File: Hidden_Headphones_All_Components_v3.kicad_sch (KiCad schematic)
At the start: 9 parts, among them SW1 SW_Push, SW2 SW_Push, U1 ESP32-S3-MINI-1, U2 PCM5102A, U3 TP4056-42-ESOP8

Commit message: worked on pcb
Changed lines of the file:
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@@
-	)
-	(symbol
-		(lib_id "power:+5V")
-		(at 36.83 45.72 0)
-		(unit 1)
-		(body_style 1)
-		(exclude_from_sim no)
-		(in_bom yes)
-		(on_board yes)
-		(in_pos_files yes)
-		(dnp no)
-		(fields_autoplaced yes)
-		(property "Reference" "#PWR01"
-			(at 36.83 49.53 0)
-			(hide yes)
-			(show_name no)
-			(do_not_autoplace no)
-			(effects
-				(font
-					(size 1.27 1.27)
-				)
-			)
-		)
-		(property "Value" "+5V"
-			(at 36.83 40.64 0)
-			(show_name no)
-			(do_not_autoplace no)
-			(effects
-				(font
-					(size 1.27 1.27)
-				)
-			)
-		)
-		(property "Footprint" ""
-			(at 36.83 45.72 0)
-			(hide yes)
-			(show_name no)
-			(do_not_autoplace no)
-			(effects
-				(font
-					(size 1.27 1.27)
-				)
-			)
-		)
-		(property "Datasheet" ""
-			(at 36.83 45.72 0)
-			(hide yes)
-			(show_name no)
-			(do_not_autoplace no)
-			(effects
-				(font
-					(size 1.27 1.27)
-				)
-			)
-		)
-		(property "Description" "Power symbol creates a global label with name \"+5V\""
-			(at 36.83 45.72 0)
-			(hide yes)
-			(show_name no)
-			(do_not_autoplace no)
-			(effects
-				(font
-					(size 1.27 1.27)
-				)
-			)
-		)
-		(pin "1"
-		)
-		(instances
-			(project "Hidden_Headphones_All_Components_v3"
-				(path "/229b286c-fec7-4b98-8d6c-8cdc215e0cc6"
-					(reference "#PWR01")
-					(unit 1)
-				)
-			)
-		)
 	)
 	(symbol

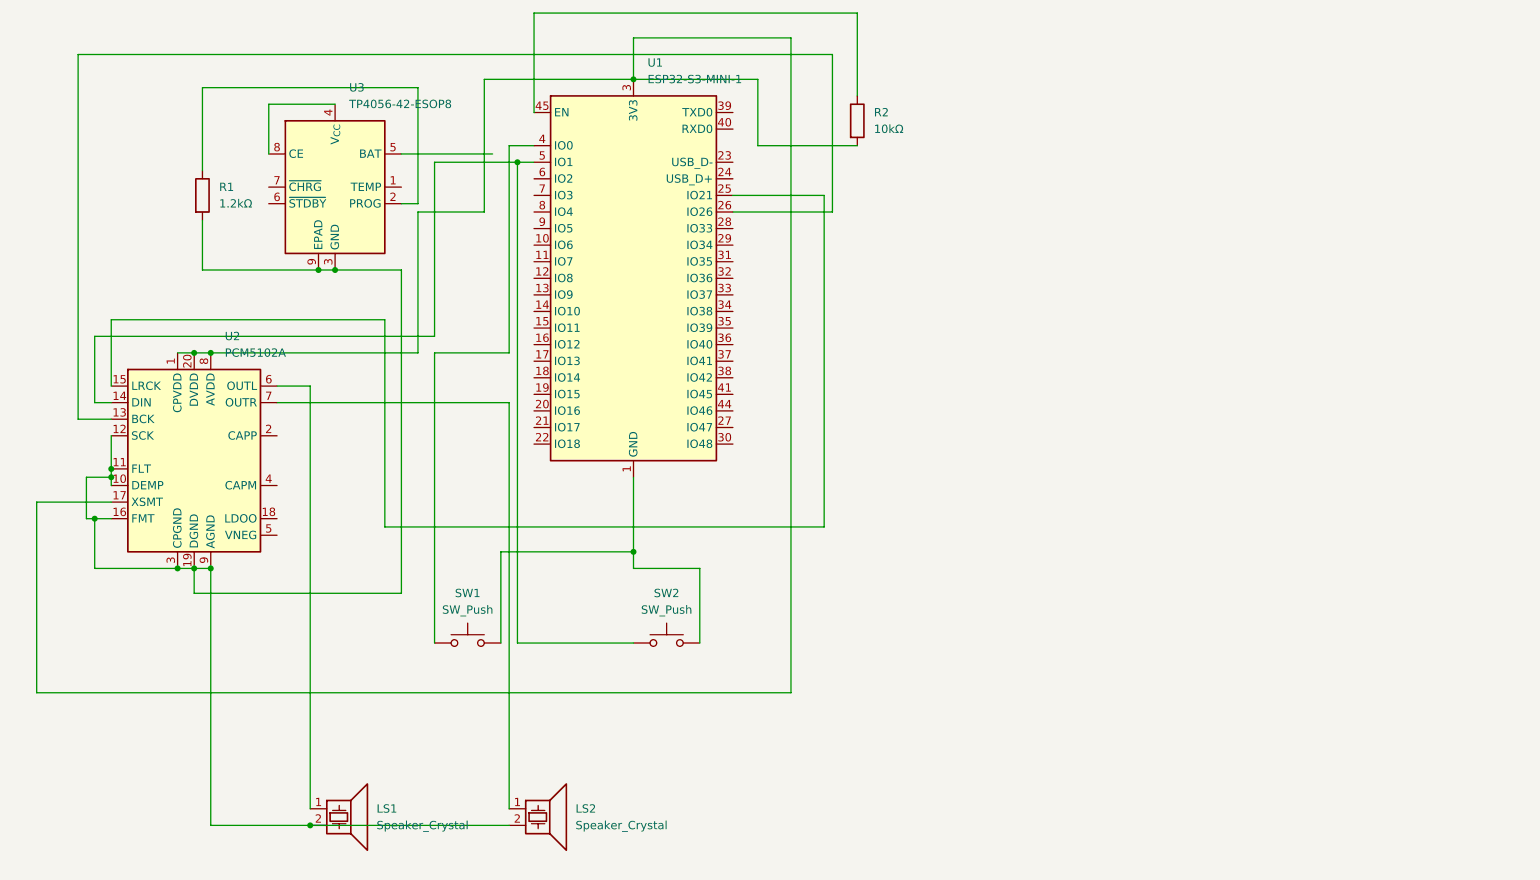
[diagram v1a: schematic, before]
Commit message: rough firmware creation and editing pcb
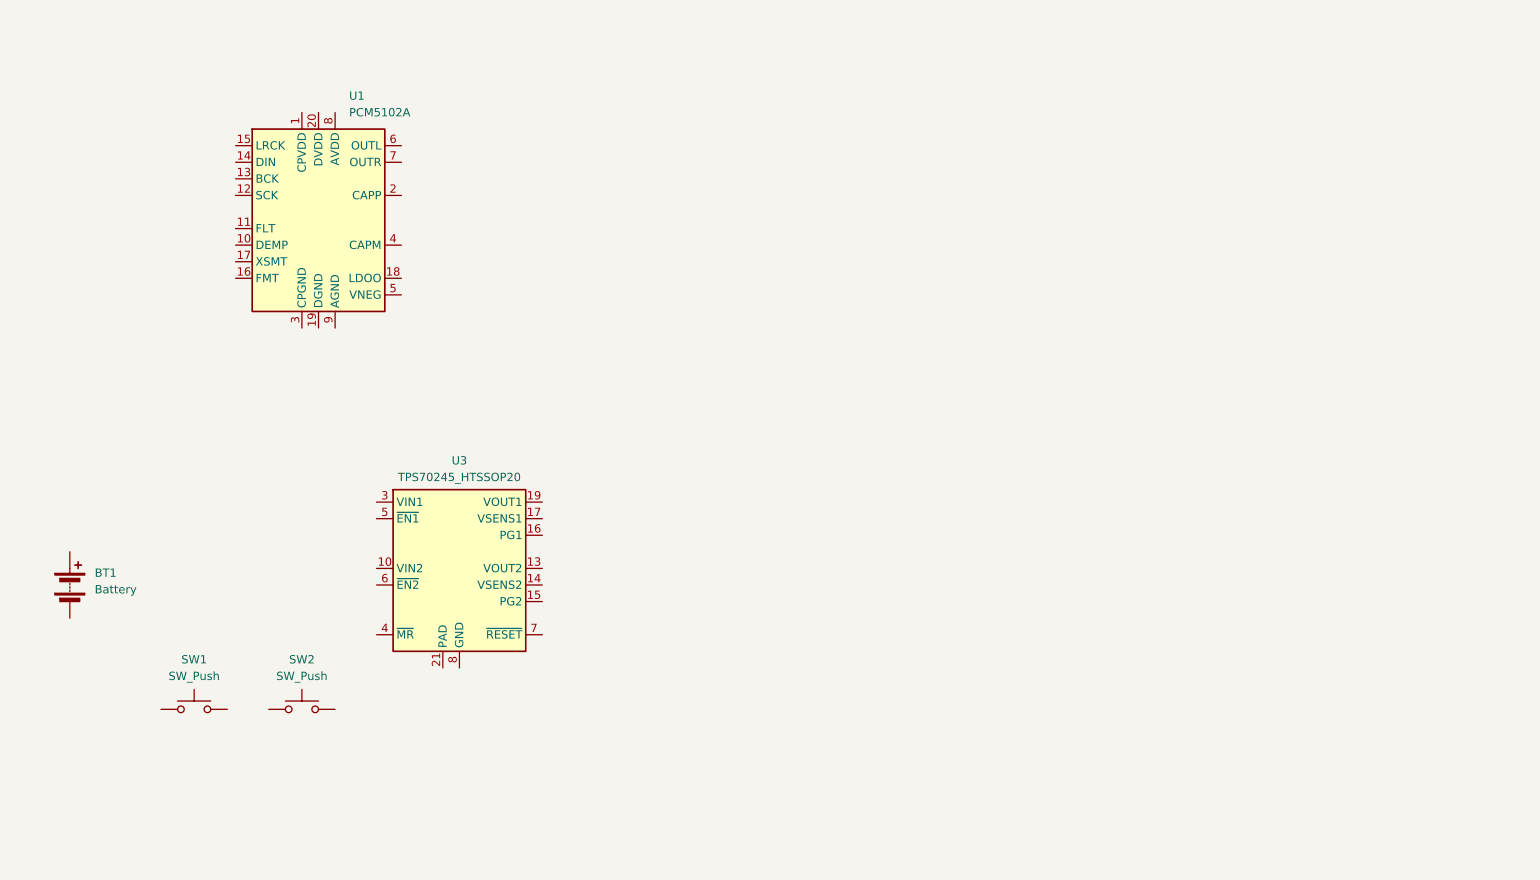
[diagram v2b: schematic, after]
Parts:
- removed LS1, LS2: Speaker_Crystal, symbol Device:Speaker_Crystal
- removed R1: 1.2kΩ, Resistor_THT:R_Axial_DIN0207_L6.3mm_D2.5mm_P7.62mm_Horizontal, symbol Device:R
- removed R2: 10kΩ, Resistor_SMD:R_0805_2012Metric, symbol Device:R
- removed U1: ESP32-S3-MINI-1, RF_Module:ESP32-S2-MINI-1, symbol RF_Module:ESP32-S3-MINI-1
- removed U2: PCM5102A, Package_SO:TSSOP-20_4.4x6.5mm_P0.65mm, symbol Audio:PCM5102A
- removed U3: TP4056-42-ESOP8, Package_SO:SOIC-8-1EP_3.9x4.9mm_P1.27mm_EP2.29x3mm, symbol Battery_Management:TP4056-42-ESOP8
- added BT1: Battery, symbol Device:Battery
- added U1: PCM5102A, Package_SO:TSSOP-20_4.4x6.5mm_P0.65mm, symbol Audio:PCM5102A
- added U3: TPS70245_HTSSOP20, Package_SO:HTSSOP-20-1EP_4.4x6.5mm_P0.65mm_EP3.4x6.5mm_ThermalVias, symbol Regulator_Linear:TPS70245_HTSSOP20
- SW1, SW2: footprint Button_Switch_THT:KSA_Tactile_SPST -> (none)
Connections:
- net at SW1.2: no longer SW2.2
- new net: U3.10 (VIN2), U3.9 (VIN2)
- new net: U3.12 (VOUT2), U3.13 (VOUT2)
- new net: U3.18 (VOUT1), U3.19 (VOUT1)
- new net: U3.2 (VIN1), U3.3 (VIN1)

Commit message: started pcb redesign, redid firmware for it
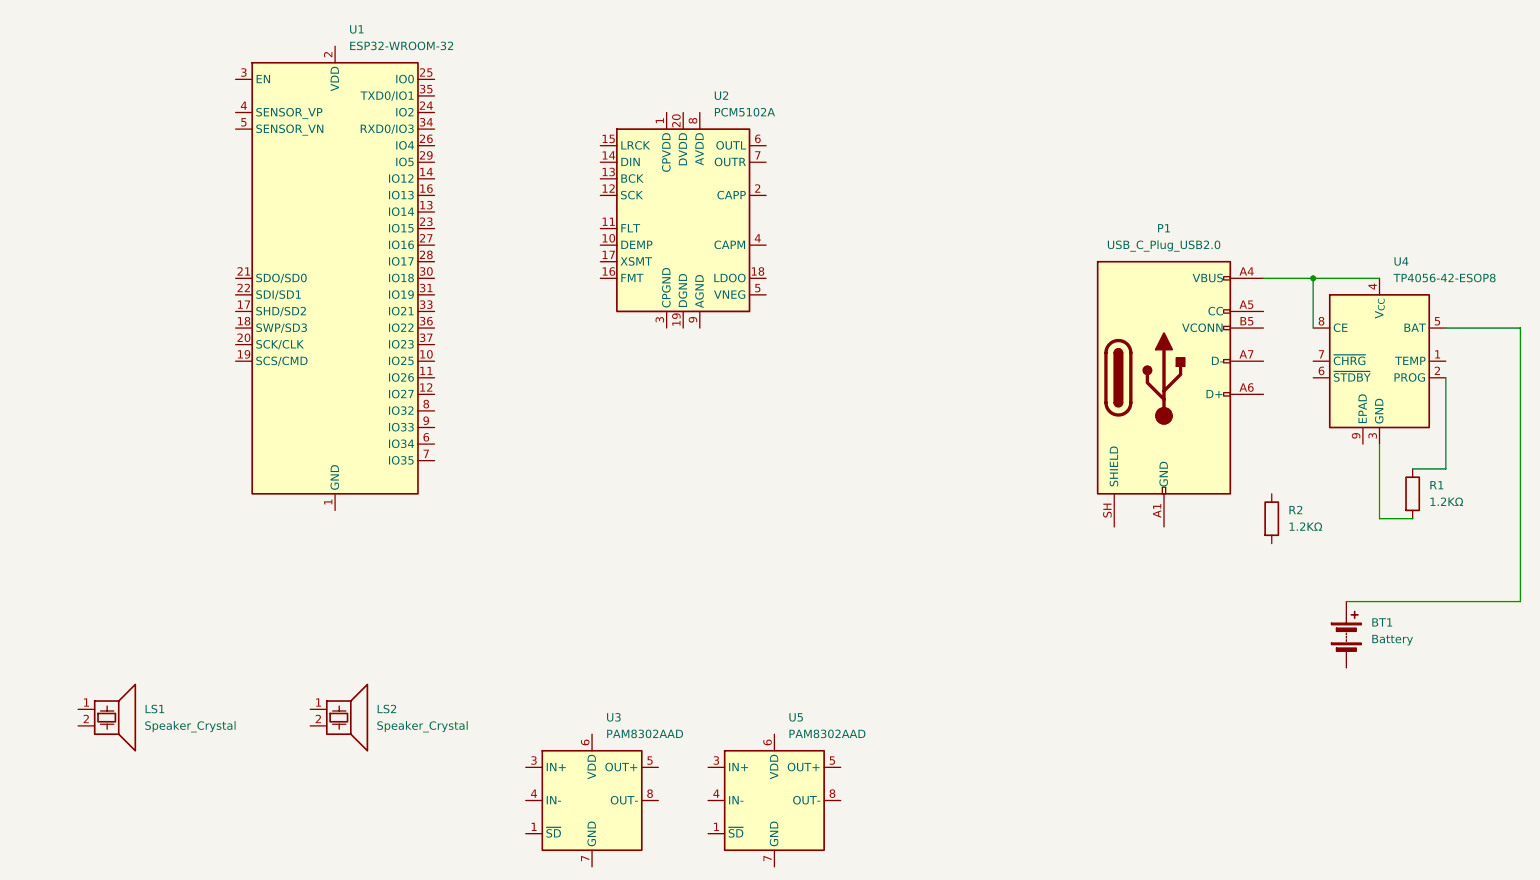
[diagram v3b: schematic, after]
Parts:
- removed SW1, SW2: SW_Push, symbol Switch:SW_Push
- removed U1: PCM5102A, Package_SO:TSSOP-20_4.4x6.5mm_P0.65mm, symbol Audio:PCM5102A
- removed U3: TPS70245_HTSSOP20, Package_SO:HTSSOP-20-1EP_4.4x6.5mm_P0.65mm_EP3.4x6.5mm_ThermalVias, symbol Regulator_Linear:TPS70245_HTSSOP20
- added LS1, LS2: Speaker_Crystal, symbol Device:Speaker_Crystal
- added P1: USB_C_Plug_USB2.0, symbol Connector:USB_C_Plug_USB2.0
- added R1, R2: 1.2KΩ, symbol Device:R
- added U1: ESP32-WROOM-32, RF_Module:ESP32-WROOM-32, symbol RF_Module:ESP32-WROOM-32
- added U2: PCM5102A, Package_SO:TSSOP-20_4.4x6.5mm_P0.65mm, symbol Audio:PCM5102A
- added U3, U5: PAM8302AAD, symbol Amplifier_Audio:PAM8302AAD
- added U4: TP4056-42-ESOP8, Package_SO:SOIC-8-1EP_3.9x4.9mm_P1.27mm_EP2.41x3.3mm_ThermalVias, symbol Battery_Management:TP4056-42-ESOP8
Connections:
- net at BT1.1 (+): now also U4.5 (BAT)
- new net: R1.1, U4.2 (PROG)
- new net: R1.2, U4.3 (GND)
- new net: P1.A4 (VBUS), P1.A9 (VBUS), P1.B4 (VBUS), P1.B9 (VBUS), U4.4 (V_{CC}), U4.8 (CE)
- new net: P1.A1 (GND), P1.A12 (GND), P1.B1 (GND), P1.B12 (GND)
- new net: U1.1 (GND), U1.15 (GND), U1.38 (GND), U1.39 (GND)
